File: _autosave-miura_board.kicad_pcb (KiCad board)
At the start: 2 copper layers, 60 x 60 mm, 40 parts, among them J1 Screw_Terminal_01x02, J2 Screw_Terminal_01x02, J3 Screw_Terminal_01x02, J4 Conn_01x04_Male, J5 Screw_Terminal_01x02, J6 Screw_Terminal_01x02, J7 Screw_Terminal_01x02, J8 Screw_Terminal_01x02, SW1 SW_Push, SW2 SW_Push, U1 ESP32-WROOM, U3 DRV8833PW, U4 DRV8833PW, U5 AMS1117, U6 MPU-6050, U7 L7806, U8 DRV8833PW

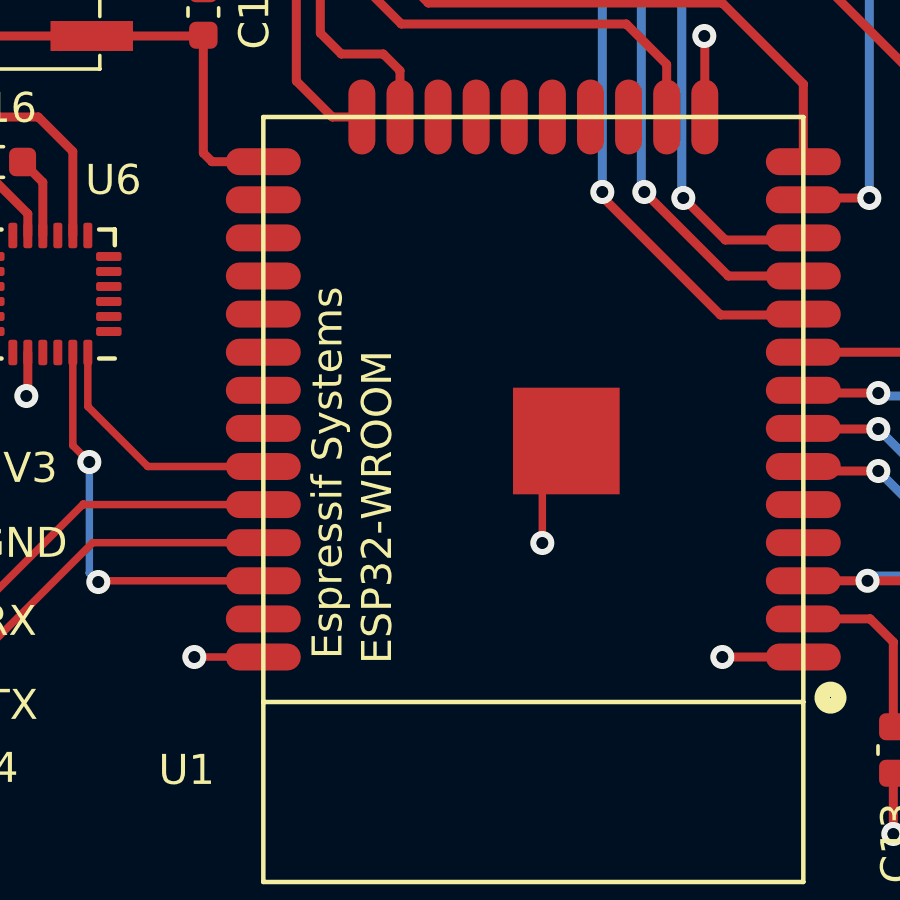
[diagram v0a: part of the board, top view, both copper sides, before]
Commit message: Ordered board, removed SPI flash
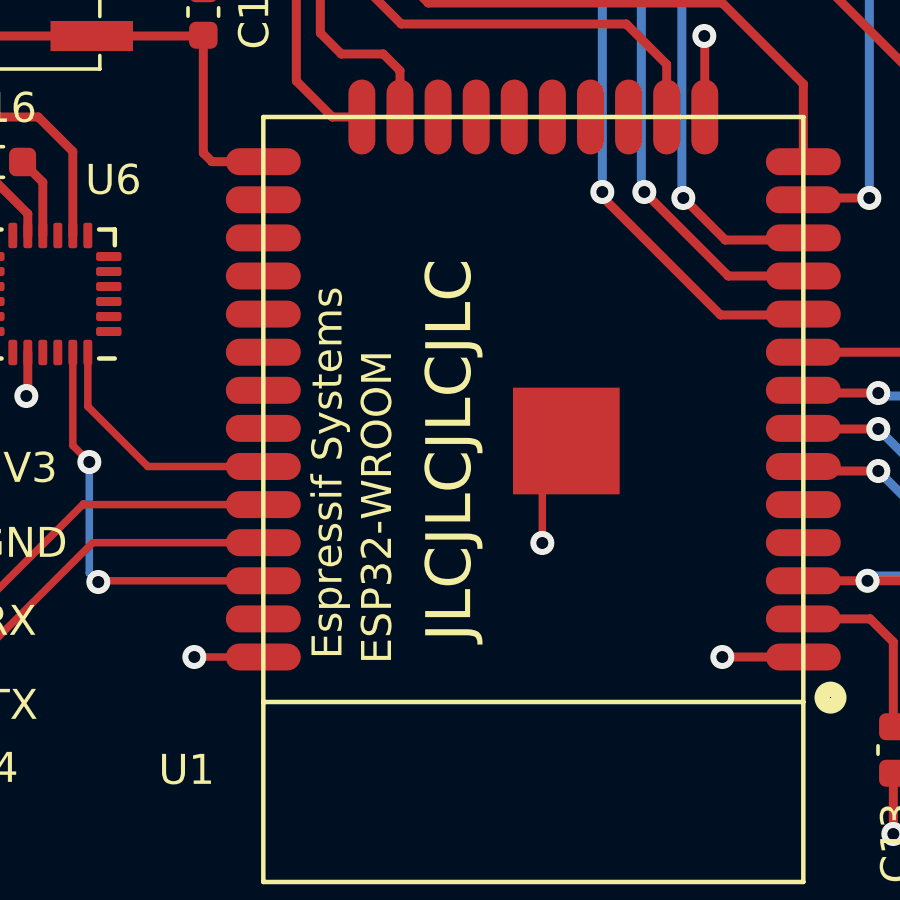
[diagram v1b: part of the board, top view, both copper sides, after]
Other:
- board text added: "JLCJLCJLCJLC"
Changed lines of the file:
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@@
       (layerselection 0x00010fc_ffffffff)
       (disableapertmacros false)
-      (usegerberextensions false)
-      (usegerberattributes true)
-      (usegerberadvancedattributes true)
-      (creategerberjobfile true)
+      (usegerberextensions true)
+      (usegerberattributes false)
+      (usegerberadvancedattributes false)
+      (creategerberjobfile false)
       (svguseinch false)
       (svgprecision 6)
@@
       (psa4output false)
       (plotreference true)
-      (plotvalue true)
+      (plotvalue false)
       (plotinvisibletext false)
       (sketchpadsonfab false)
-      (subtractmaskfromsilk false)
+      (subtractmaskfromsilk true)
       (outputformat 1)
       (mirror false)
-      (drillshape 1)
+      (drillshape 0)
       (scaleselection 1)
-      (outputdirectory "")
+      (outputdirectory "assembly/")
     )
   )
@@
     (effects (font (size 4 4) (thickness 0.15)))
   )
+  (gr_text "JLCJLCJLCJLC" (at 81.2 69.8 90) (layer "F.SilkS")
+    (effects (font (size 1.5 1.5) (thickness 0.3)))
+  )
   (gr_text "3V3\n" (at 66.8 70.4) (layer "F.SilkS")
